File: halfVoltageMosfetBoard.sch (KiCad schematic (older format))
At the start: 49 parts, among them J1 Phoenix 1987740, J2 Phoenix 1987740, J5 Phoenix 1729018, Q1 Q_NMOS_DGS, Q2 Q_NMOS_DGS, U1 STM32L011F3Px, U2 MCP1703A-3302_SOT89, U3 XC6702-3.3, U4 MIC4126

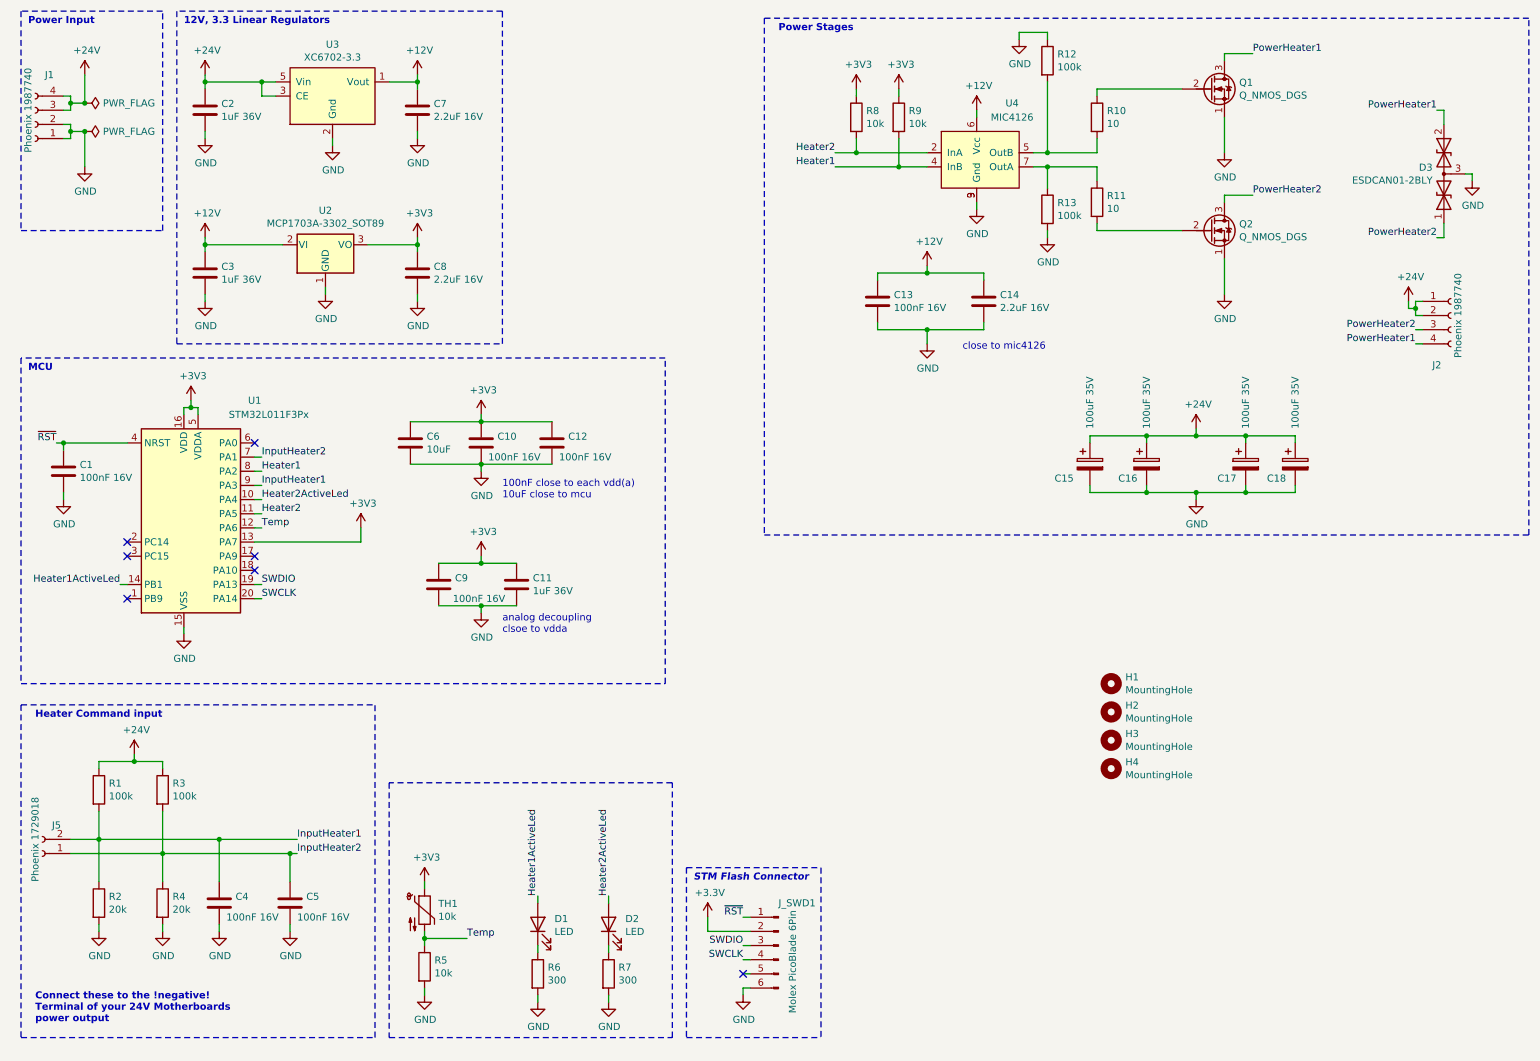
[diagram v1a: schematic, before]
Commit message: Revision 2 changes see readme Added text to readme Exported schematic
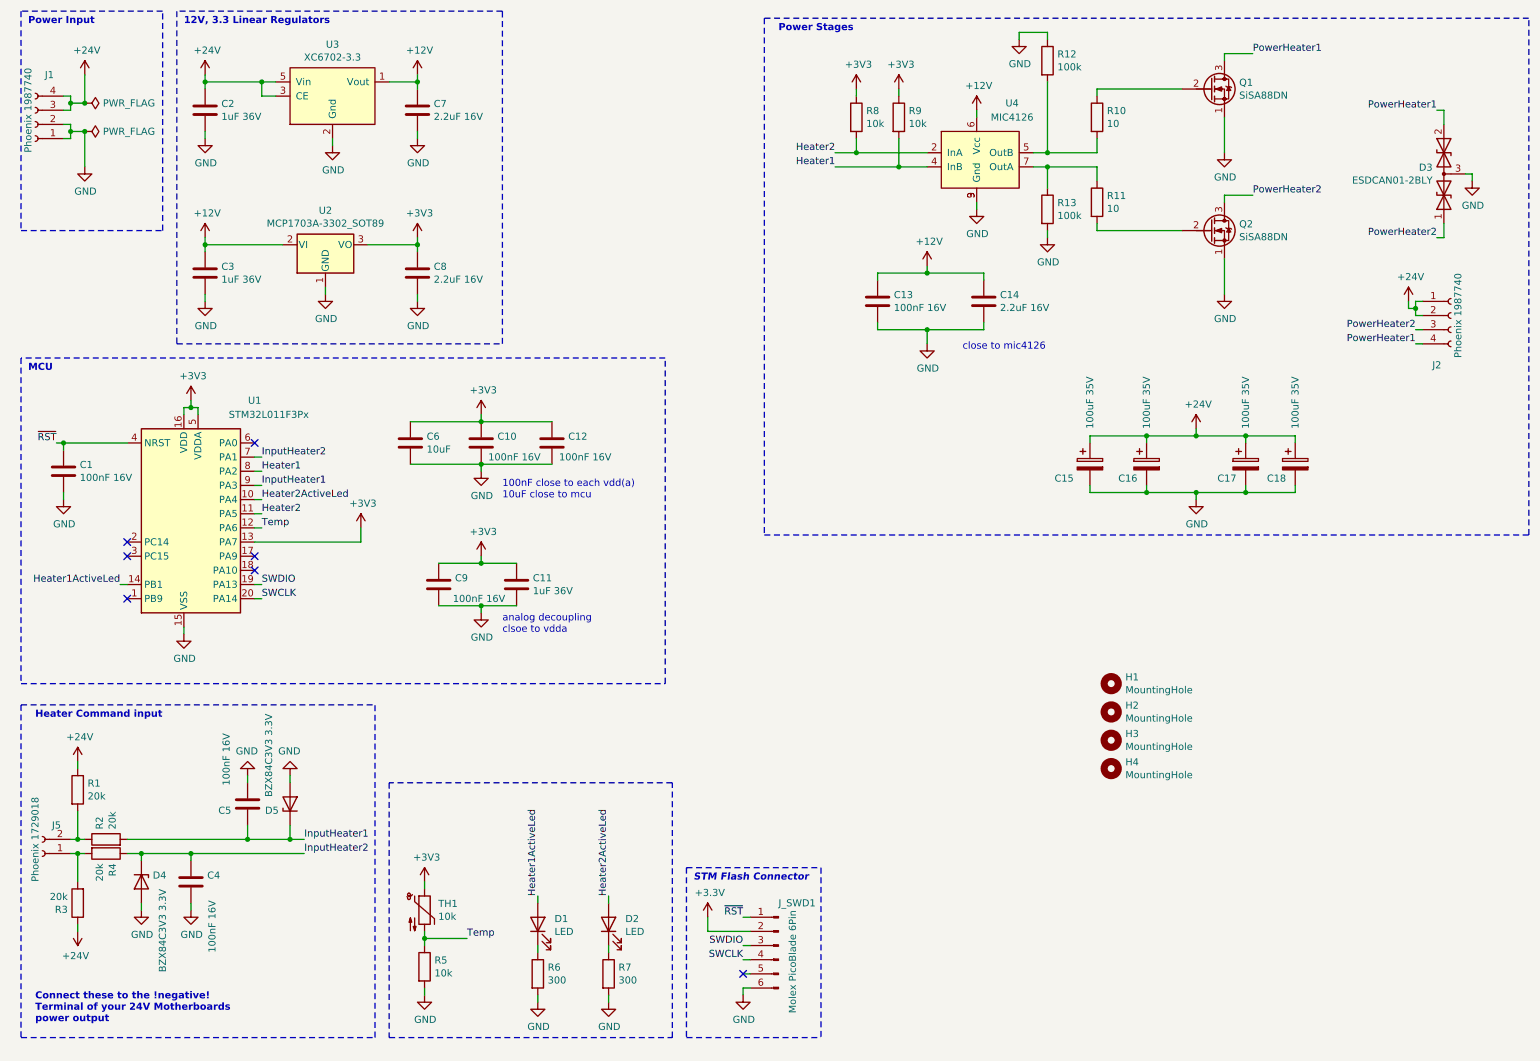
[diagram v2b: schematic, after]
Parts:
- added D4, D5: BZX84C3V3 3.3V, Diode_SMD:D_SOT-23_ANK, symbol Device:D_Zener
- Q1, Q2: value Q_NMOS_DGS -> SiSA88DN
- R1, R3: value 100k -> 20k
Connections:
- net GND: now also D4.2 (A), D5.2 (A); no longer R2.2, R4.2
- net InputHeater1: now also C5.1, R2.2, D5.1 (K); no longer C4.1, J5.2 (Pin_2), R1.2, R2.1
- net InputHeater2: now also C4.1, D4.1 (K); no longer C5.1, J5.1 (Pin_1), R3.2
- new net: J5.2 (Pin_2), R1.2, R2.1
- new net: J5.1 (Pin_1), R3.2, R4.2
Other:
- moved on the sheet: C4, C5, R1, R2, R3, R4
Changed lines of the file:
@@
 P 8900 1050
 F 0 "Q1" H 9104 1096 50  0000 L CNN
-F 1 "Q_NMOS_DGS" H 9104 1005 50  0000 L CNN
+F 1 "SiSA88DN" H 9104 1005 50  0000 L CNN
 F 2 "3dPrinterHalfVoltageMosfetBoard:Vishay_PowerPAK_1212-8_Single" H 9100 1150 50  0001 C CNN
 F 3 "~" H 8900 1050 50  0001 C CNN
@@
 P 8900 2050
 F 0 "Q2" H 9104 2096 50  0000 L CNN
-F 1 "Q_NMOS_DGS" H 9104 2005 50  0000 L CNN
+F 1 "SiSA88DN" H 9104 2005 50  0000 L CNN
 F 2 "3dPrinterHalfVoltageMosfetBoard:Vishay_PowerPAK_1212-8_Single" H 9100 2150 50  0001 C CNN
 F 3 "~" H 8900 2050 50  0001 C CNN
@@
 L power:+24V #PWR0139
 U 1 1 60C93618
-P 1300 5750
-F 0 "#PWR0139" H 1300 5600 50  0001 C CNN
-F 1 "+24V" H 1315 5923 50  0000 C CNN
-F 2 "" H 1300 5750 50  0001 C CNN
-F 3 "" H 1300 5750 50  0001 C CNN
-	1    1300 5750
-	1    0    0    -1
+P 900 7000
+F 0 "#PWR0139" H 900 6850 50  0001 C CNN
+F 1 "+24V" H 915 7173 50  0000 C CNN
+F 2 "" H 900 7000 50  0001 C CNN
+F 3 "" H 900 7000 50  0001 C CNN
+	1    900  7000
+	-1   0    0    1
 $EndComp
 $Comp
 L Device:R R1
 U 1 1 60C94098
-P 1050 6000
-F 0 "R1" H 1120 6046 50  0000 L CNN
-F 1 "100k" H 1120 5955 50  0000 L CNN
-F 2 "Resistor_SMD:R_0603_1608Metric" V 980 6000 50  0001 C CNN
-F 3 "~" H 1050 6000 50  0001 C CNN
-	1    1050 6000
-	1    0    0    -1
-$EndComp
-Wire Wire Line
-	1050 5850 1050 5800
+P 900 6000
+F 0 "R1" H 970 6046 50  0000 L CNN
+F 1 "20k" H 970 5955 50  0000 L CNN
+F 2 "Resistor_SMD:R_0603_1608Metric" V 830 6000 50  0001 C CNN
+F 3 "~" H 900 6000 50  0001 C CNN
+	1    900  6000
+	1    0    0    -1
+$EndComp
 $Comp
 L Connector:Conn_01x02_Female J5
@@
 L Device:R R3
 U 1 1 60CB2EB6
-P 1500 6000
-F 0 "R3" H 1570 6046 50  0000 L CNN
-F 1 "100k" H 1570 5955 50  0000 L CNN
-F 2 "Resistor_SMD:R_0603_1608Metric" V 1430 6000 50  0001 C CNN
-F 3 "~" H 1500 6000 50  0001 C CNN
-	1    1500 6000
-	1    0    0    -1
-$EndComp
-Wire Wire Line
-	1050 5800 1300 5800
-Wire Wire Line
-	1500 5800 1500 5850
-Wire Wire Line
-	1300 5800 1300 5750
-Connection ~ 1300 5800
-Wire Wire Line
-	1300 5800 1500 5800
-Wire Wire Line
-	850  6350 1050 6350
-Wire Wire Line
-	850  6450 1500 6450
-Wire Wire Line
-	1050 6150 1050 6350
-Connection ~ 1050 6350
-Wire Wire Line
-	1500 6150 1500 6450
-Connection ~ 1500 6450
-Wire Wire Line
-	1050 6350 1050 6650
+P 900 6800
+F 0 "R3" H 970 6846 50  0000 L CNN
+F 1 "20k" H 970 6755 50  0000 L CNN
+F 2 "Resistor_SMD:R_0603_1608Metric" V 830 6800 50  0001 C CNN
+F 3 "~" H 900 6800 50  0001 C CNN
+	1    900  6800
+	-1   0    0    1
+$EndComp
 $Comp
 L Device:R R2
 U 1 1 60CF24AB
-P 1050 6800
-F 0 "R2" H 1120 6846 50  0000 L CNN
-F 1 "20k" H 1120 6755 50  0000 L CNN
-F 2 "Resistor_SMD:R_0603_1608Metric" V 980 6800 50  0001 C CNN
-F 3 "~" H 1050 6800 50  0001 C CNN
-	1    1050 6800
-	1    0    0    -1
+P 1100 6350
+F 0 "R2" H 1170 6396 50  0000 L CNN
+F 1 "20k" H 1170 6305 50  0000 L CNN
+F 2 "Resistor_SMD:R_0603_1608Metric" V 1030 6350 50  0001 C CNN
+F 3 "~" H 1100 6350 50  0001 C CNN
+	1    1100 6350
+	0    -1   -1   0
 $EndComp
 $Comp
 L Device:R R4
 U 1 1 60CF2775
-P 1500 6800
-F 0 "R4" H 1570 6846 50  0000 L CNN
-F 1 "20k" H 1570 6755 50  0000 L CNN
-F 2 "Resistor_SMD:R_0603_1608Metric" V 1430 6800 50  0001 C CNN
-F 3 "~" H 1500 6800 50  0001 C CNN
-	1    1500 6800
-	1    0    0    -1
-$EndComp
-Wire Wire Line
-	1500 6450 1500 6650
+P 1100 6450
+F 0 "R4" H 1170 6496 50  0000 L CNN
+F 1 "20k" H 1170 6405 50  0000 L CNN
+F 2 "Resistor_SMD:R_0603_1608Metric" V 1030 6450 50  0001 C CNN
+F 3 "~" H 1100 6450 50  0001 C CNN
+	1    1100 6450
+	0    1    1    0
+$EndComp
 $Comp
 L power:GND #PWR0140
 U 1 1 60CFAF9F
-P 1050 7000
-F 0 "#PWR0140" H 1050 6750 50  0001 C CNN
-F 1 "GND" H 1055 6827 50  0000 C CNN
-F 2 "" H 1050 7000 50  0001 C CNN
-F 3 "" H 1050 7000 50  0001 C CNN
-	1    1050 7000
-	1    0    0    -1
-$EndComp
-Wire Wire Line
-	1050 7000 1050 6950
+P 1350 6850
+F 0 "#PWR0140" H 1350 6600 50  0001 C CNN
+F 1 "GND" H 1355 6677 50  0000 C CNN
+F 2 "" H 1350 6850 50  0001 C CNN
+F 3 "" H 1350 6850 50  0001 C CNN
+	1    1350 6850
+	1    0    0    -1
+$EndComp
+Wire Wire Line
+	1350 6850 1350 6800
 $Comp
 L power:GND #PWR0141
 U 1 1 60D039F0
-P 1500 7000
-F 0 "#PWR0141" H 1500 6750 50  0001 C CNN
-F 1 "GND" H 1505 6827 50  0000 C CNN
-F 2 "" H 1500 7000 50  0001 C CNN
-F 3 "" H 1500 7000 50  0001 C CNN
-	1    1500 7000
-	1    0    0    -1
-$EndComp
-Wire Wire Line
-	1500 7000 1500 6950
+P 2400 5900
+F 0 "#PWR0141" H 2400 5650 50  0001 C CNN
+F 1 "GND" H 2405 5727 50  0000 C CNN
+F 2 "" H 2400 5900 50  0001 C CNN
+F 3 "" H 2400 5900 50  0001 C CNN
+	1    2400 5900
+	-1   0    0    1
+$EndComp
+Wire Wire Line
+	2400 5900 2400 5950
 Text Notes 600  7650 0    50   ~ 10
 Connect these to the !negative! \nTerminal of your 24V Motherboards \npower output
@@
 L Device:C C4
 U 1 1 60D97ABF
-P 1900 6800
-F 0 "C4" H 2015 6846 50  0000 L CNN
-F 1 "100nF 16V" H 1950 6700 50  0000 L CNN
-F 2 "Capacitor_SMD:C_0603_1608Metric" H 1938 6650 50  0001 C CNN
-F 3 "~" H 1900 6800 50  0001 C CNN
-	1    1900 6800
+P 1700 6650
+F 0 "C4" H 1815 6696 50  0000 L CNN
+F 1 "100nF 16V" V 1850 6150 50  0000 L CNN
+F 2 "Capacitor_SMD:C_0603_1608Metric" H 1738 6500 50  0001 C CNN
+F 3 "~" H 1700 6650 50  0001 C CNN
+	1    1700 6650
 	1    0    0    -1
 $EndComp
@@
 L Device:C C5
 U 1 1 60D98146
-P 2400 6800
-F 0 "C5" H 2515 6846 50  0000 L CNN
-F 1 "100nF 16V" H 2450 6700 50  0000 L CNN
-F 2 "Capacitor_SMD:C_0603_1608Metric" H 2438 6650 50  0001 C CNN
-F 3 "~" H 2400 6800 50  0001 C CNN
-	1    2400 6800
-	1    0    0    -1
+P 2100 6100
+F 0 "C5" H 2215 6146 50  0000 L CNN
+F 1 "100nF 16V" V 2250 5600 50  0000 L CNN
+F 2 "Capacitor_SMD:C_0603_1608Metric" H 2138 5950 50  0001 C CNN
+F 3 "~" H 2100 6100 50  0001 C CNN
+	1    2100 6100
+	-1   0    0    1
 $EndComp
 $Comp
 L power:GND #PWR0142
 U 1 1 60D98434
-P 1900 7000
-F 0 "#PWR0142" H 1900 6750 50  0001 C CNN
-F 1 "GND" H 1905 6827 50  0000 C CNN
-F 2 "" H 1900 7000 50  0001 C CNN
-F 3 "" H 1900 7000 50  0001 C CNN
-	1    1900 7000
+P 1700 6850
+F 0 "#PWR0142" H 1700 6600 50  0001 C CNN
+F 1 "GND" H 1705 6677 50  0000 C CNN
+F 2 "" H 1700 6850 50  0001 C CNN
+F 3 "" H 1700 6850 50  0001 C CNN
+	1    1700 6850
 	1    0    0    -1
 $EndComp
@@
 L power:GND #PWR0143
 U 1 1 60D98566
-P 2400 7000
-F 0 "#PWR0143" H 2400 6750 50  0001 C CNN
-F 1 "GND" H 2405 6827 50  0000 C CNN
-F 2 "" H 2400 7000 50  0001 C CNN
-F 3 "" H 2400 7000 50  0001 C CNN
-	1    2400 7000
-	1    0    0    -1
-$EndComp
-Wire Wire Line
-	2400 6950 2400 7000
-Wire Wire Line
-	1900 6950 1900 7000
-Wire Wire Line
-	1500 6450 2400 6450
-Wire Wire Line
-	1050 6350 1900 6350
-Wire Wire Line
-	1900 6650 1900 6350
-Connection ~ 1900 6350
-Wire Wire Line
-	1900 6350 2450 6350
-Wire Wire Line
-	2400 6450 2400 6650
-Connection ~ 2400 6450
-Wire Wire Line
-	2400 6450 2450 6450
+P 2100 5900
+F 0 "#PWR0143" H 2100 5650 50  0001 C CNN
+F 1 "GND" H 2105 5727 50  0000 C CNN
+F 2 "" H 2100 5900 50  0001 C CNN
+F 3 "" H 2100 5900 50  0001 C CNN
+	1    2100 5900
+	-1   0    0    1
+$EndComp
+Wire Wire Line
+	2100 5950 2100 5900
+Wire Wire Line
+	1700 6800 1700 6850
 Wire Notes Line
 	3000 7750 3000 5400
@@
 Wire Wire Line
 	2200 3950 2150 3950
-Text Label 2450 6450 0    50   ~ 0
+Text Label 2500 6450 0    50   ~ 0
 InputHeater2
-Text Label 2450 6350 0    50   ~ 0
+Text Label 2500 6350 0    50   ~ 0
 InputHeater1
+$Comp
+L Device:D_Zener D4
+U 1 1 609C9858
+P 1350 6650
+F 0 "D4" V 1304 6730 50  0000 L CNN
+F 1 "BZX84C3V3 3.3V" H 1400 6800 50  0000 L CNN
+F 2 "Diode_SMD:D_SOT-23_ANK" H 1350 6650 50  0001 C CNN
+F 3 "~" H 1350 6650 50  0001 C CNN
+	1    1350 6650
+	0    1    1    0
+$EndComp
+Wire Wire Line
+	1250 6450 1350 6450
+Wire Wire Line
+	1350 6450 1350 6500
+Connection ~ 1350 6450
+$Comp
+L Device:D_Zener D5
+U 1 1 60A234DB
+P 2400 6100
+F 0 "D5" V 2354 6180 50  0000 L CNN
+F 1 "BZX84C3V3 3.3V" H 2450 6250 50  0000 L CNN
+F 2 "Diode_SMD:D_SOT-23_ANK" H 2400 6100 50  0001 C CNN
+F 3 "~" H 2400 6100 50  0001 C CNN
+	1    2400 6100
+	0    -1   -1   0
+$EndComp
+Wire Wire Line
+	1700 6500 1700 6450
+Connection ~ 1700 6450
+Wire Wire Line
+	1700 6450 2500 6450
+$Comp
+L power:+24V #PWR0146
+U 1 1 60AD6855
+P 900 5800
+F 0 "#PWR0146" H 900 5650 50  0001 C CNN
+F 1 "+24V" H 915 5973 50  0000 C CNN
+F 2 "" H 900 5800 50  0001 C CNN
+F 3 "" H 900 5800 50  0001 C CNN
+	1    900  5800
+	1    0    0    -1
+$EndComp
+Wire Wire Line
+	900  5800 900  5850
+Wire Wire Line
+	900  6950 900  7000
+Wire Wire Line
+	1350 6450 1700 6450
+Wire Wire Line
+	850  6350 900  6350
+Wire Wire Line
+	850  6450 900  6450
+Wire Wire Line
+	900  6650 900  6450
+Connection ~ 900  6450
+Wire Wire Line
+	900  6450 950  6450
+Wire Wire Line
+	900  6150 900  6350
+Connection ~ 900  6350
+Wire Wire Line
+	900  6350 950  6350
+Wire Wire Line
+	1250 6350 2100 6350
+Wire Wire Line
+	2400 6350 2400 6250
+Connection ~ 2400 6350
+Wire Wire Line
+	2400 6350 2500 6350
+Wire Wire Line
+	2100 6250 2100 6350
+Connection ~ 2100 6350
+Wire Wire Line
+	2100 6350 2400 6350
 $EndSCHEMATC
